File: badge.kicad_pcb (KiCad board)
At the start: 2 copper layers, 65 x 75 mm, 21 parts, among them J1 PMOD_0, J2 PMOD_1, U1 TPS61165

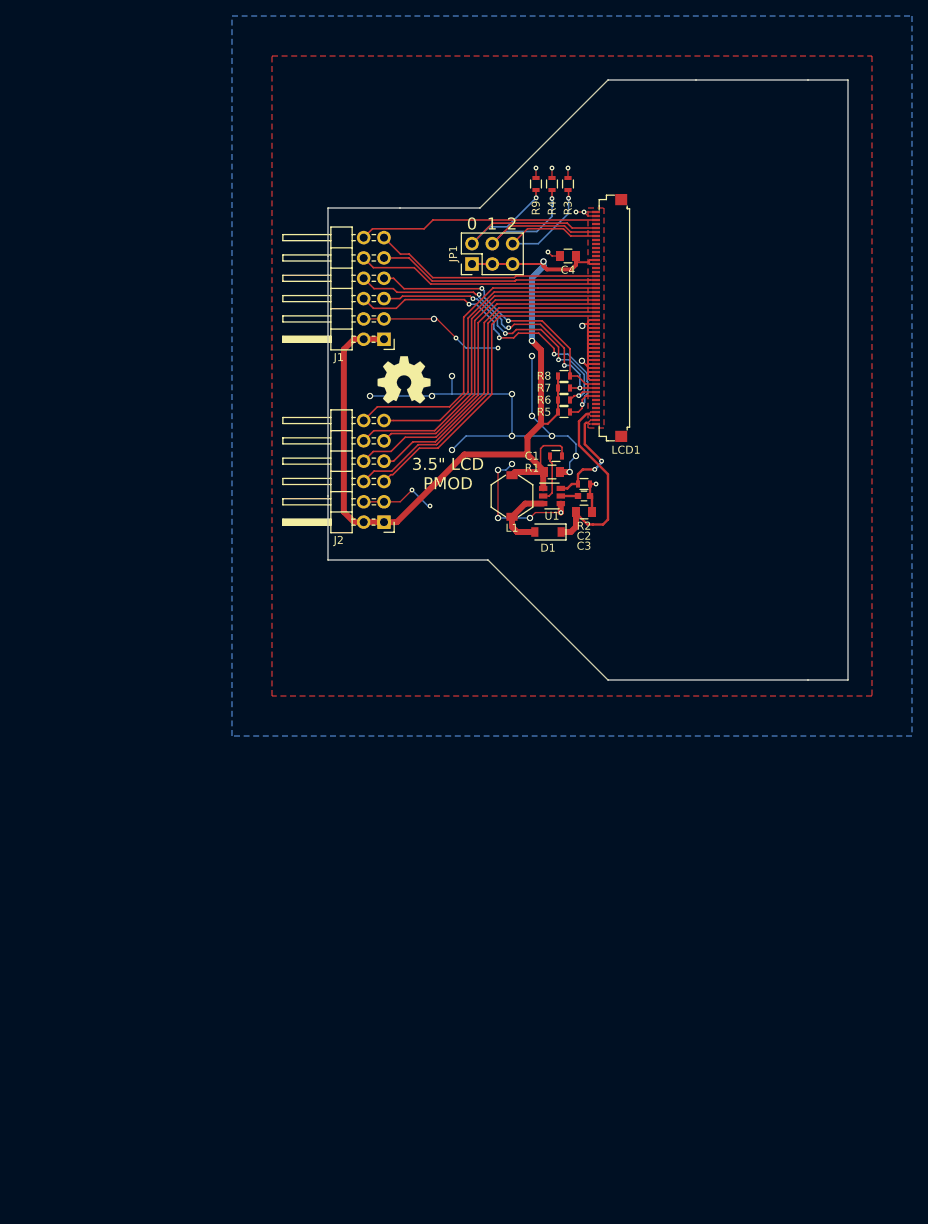
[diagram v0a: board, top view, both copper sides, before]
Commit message: Footprint assignments and initial placement
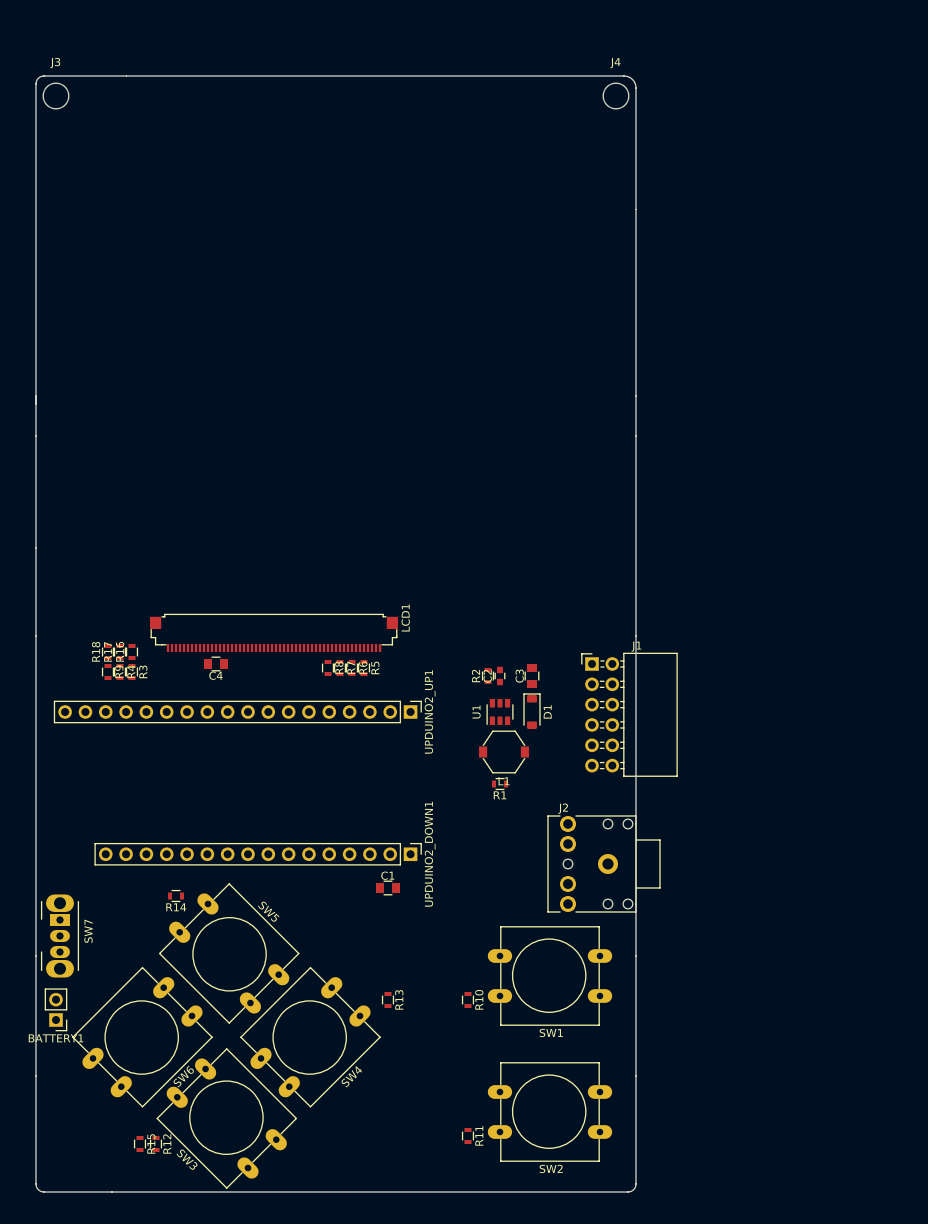
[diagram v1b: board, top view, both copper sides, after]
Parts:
- removed JP1: JMPx3, Pin_Headers:Pin_Header_Straight_2x03_Pitch2.54mm
- removed REF***: OSHW-Symbol_6.7x6mm_SilkScreen, Symbols:OSHW-Symbol_6.7x6mm_SilkScreen
- added BATTERY1: Conn_01x02, Pin_Headers:Pin_Header_Straight_1x02_Pitch2.54mm, F.Cu at (73.0, 150.5)
- added J3: HOLE, Mounting_Holes:MountingHole_3.2mm_M3, F.Cu at (73.0, 35.0)
- added J4: HOLE, Mounting_Holes:MountingHole_3.2mm_M3, F.Cu at (143.0, 35.0)
- added R10: 10K, Resistors_SMD:R_0603, F.Cu at (124.5, 148.0)
- added R11: 10K, Resistors_SMD:R_0603, F.Cu at (124.5, 165.0)
- added R12: 10K, Resistors_SMD:R_0603, F.Cu at (85.5, 166.0)
- added R13: 10K, Resistors_SMD:R_0603, F.Cu at (114.5, 148.0)
- added R14: 10K, Resistors_SMD:R_0603, F.Cu at (88.0, 135.0)
- added R15: 10K, Resistors_SMD:R_0603, F.Cu at (83.5, 166.0)
- added R16: DNP, Resistors_SMD:R_0603, F.Cu at (82.5, 104.5)
- added R17: DNP, Resistors_SMD:R_0603, F.Cu at (81.0, 104.5)
- added R18: 10k, Resistors_SMD:R_0603, F.Cu at (79.5, 104.5)
- added SW1: SW_Push, Buttons_Switches_THT:SW_PUSH-12mm, F.Cu at (141.0, 147.5)
- added SW2: SW_Push, Buttons_Switches_THT:SW_PUSH-12mm, F.Cu at (141.0, 164.5)
- added SW3: SW_Push, Buttons_Switches_THT:SW_PUSH-12mm, F.Cu at (97.0, 169.0)
- added SW4: SW_Push, Buttons_Switches_THT:SW_PUSH-12mm, F.Cu at (111.0, 150.0)
- added SW5: SW_Push, Buttons_Switches_THT:SW_PUSH-12mm, F.Cu at (92.0, 136.0)
- added SW6: SW_Push, Buttons_Switches_THT:SW_PUSH-12mm, F.Cu at (90.0, 150.0)
- added SW7: SW_SPDT, Buttons_Switches_THT:SW_CuK_OS102011MA1QN1_SPDT_Angled, F.Cu at (73.5, 138.0)
- added UPDUINO2_DOWN1: Conn_01x16, Pin_Headers:Pin_Header_Straight_1x16_Pitch2.54mm, F.Cu at (117.3, 129.8)
- added UPDUINO2_UP1: Conn_01x18, Pin_Headers:Pin_Header_Straight_1x18_Pitch2.54mm, F.Cu at (117.3, 112.0)
- J1: value PMOD_0 -> PMOD; footprint Custom Parts:PMOD_2x06_2.54mm -> Custom Parts:Pin_Header_Angled_2x06_Pitch2.54mm_PMOD
- J2: value PMOD_1 -> Audio-Jack-3; footprint Custom Parts:PMOD_2x06_2.54mm -> Custom Parts:AUDIO_JACK_3.5mm
- R9: value 10k -> DNP
- moved R3 81.8 mm to (82.5, 107.0), turned to 270 degrees
- moved R4 81.5 mm to (81.0, 107.0), turned to 270 degrees
- moved R9 81.1 mm to (79.5, 107.0), turned to 270 degrees
- moved C4 67.4 mm to (93.0, 106.0)
- moved LCD1 57.6 mm to (100.2, 103.5), turned to 180 degrees
- moved C1 55.9 mm to (114.5, 134.0)
- moved J2 51.1 mm to (142.0, 131.0)
- moved J1 48.2 mm to (140.0, 106.0), turned to 0 degrees
- moved R8 46.9 mm to (107.0, 106.5), turned to 270 degrees
- moved R7 44.8 mm to (108.5, 106.5), turned to 270 degrees
- moved R6 42.7 mm to (110.0, 106.5), turned to 270 degrees
- moved R1 41.6 mm to (128.5, 121.0), turned to 180 degrees
- moved R5 40.6 mm to (111.5, 106.5), turned to 270 degrees
- moved L1 32.0 mm to (129.0, 117.0), turned to 0 degrees
- moved U1 27.8 mm to (128.5, 112.0), turned to 90 degrees
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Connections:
- net Net-(R1-Pad1) renamed /TPS_CTRL
- J1 pad 1: /DCLK -> /PMOD0
- J1 pad 10: /~RESET -> /PMOD7
- J1 pad 2: /VSYNC -> /PMOD2
- J1 pad 3: /SPDAT -> /PMOD4
- J1 pad 4: /SPENA -> /PMOD6
- J1 pad 7: /DEN -> /PMOD1
- J1 pad 8: /HSYNC -> /PMOD3
- J1 pad 9: /SPCLK -> /PMOD5
- J2 pad 1: /DX6 -> /AUDIO
- J2 pad 2: /DX4 -> /AUDIO
- J2 pad 3: /DX2 -> GND
- LCD1 pad 10: /SPCLK -> Net-(LCD1-Pad10)
- LCD1 pad 11: /SPDAT -> Net-(LCD1-Pad11)
- LCD1 pad 39: Net-(LCD1-Pad39) -> (no net)
- LCD1 pad 40: Net-(LCD1-Pad40) -> (no net)
- LCD1 pad 43: Net-(LCD1-Pad43) -> (no net)
- LCD1 pad 44: Net-(LCD1-Pad44) -> (no net)
- LCD1 pad 45: Net-(LCD1-Pad45) -> (no net)
- LCD1 pad 46: Net-(LCD1-Pad46) -> (no net)
- LCD1 pad 47: Net-(LCD1-Pad47) -> (no net)
- LCD1 pad 5: Net-(LCD1-Pad5) -> (no net)
- LCD1 pad 51: Net-(LCD1-Pad51) -> (no net)
- LCD1 pad 6: Net-(LCD1-Pad6) -> (no net)
- LCD1 pad 7: Net-(LCD1-Pad7) -> (no net)
- LCD1 pad 9: /SPENA -> Net-(LCD1-Pad9)
- R6 pad 1: /SPENA -> Net-(LCD1-Pad9)
- R7 pad 1: /SPCLK -> Net-(LCD1-Pad10)
- R8 pad 1: /SPDAT -> Net-(LCD1-Pad11)
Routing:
- net GND: track 143.0 -> 0.00 mm, vias 30 -> 0
- net +3V3: track 121.3 -> 0.00 mm, vias 2 -> 0
- net /~RESET: track 43.3 -> 0.00 mm, vias 4 -> 0
- net /DX1: track 42.9 -> 0.00 mm
- net /DX3: track 42.5 -> 0.00 mm
- net /DX5: track 42.0 -> 0.00 mm
- net /DX7: track 41.4 -> 0.00 mm
- net /DX0: track 40.2 -> 0.00 mm
- net /DX2: track 39.6 -> 0.00 mm
- net /DX4: track 39.2 -> 0.00 mm
- net /SPCLK: track 39.1 -> 0.00 mm, vias 4 -> 0
- net /DX6: track 38.6 -> 0.00 mm
- net /SPENA: track 37.8 -> 0.00 mm, vias 4 -> 0
- net /SPDAT: track 34.5 -> 0.00 mm, vias 2 -> 0
- net /HSYNC: track 30.4 -> 0.00 mm
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- removed copper zone on B.Cu, net GND
- removed copper zone on F.Cu, net GND
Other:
- board size 65 x 75 mm -> 75 x 139.5 mm
- board text removed: "0"
- board text removed: "1"
- board text removed: "2"
- board text removed: "3.5" LCD PMOD"

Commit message: Routing done and logos added
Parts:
- added J11: ICESTUDIO_LOGO, Custom Parts:ICESTUDIO, B.Cu at (126.8, 82.5)
- added J5: OSHW_LOGO, Symbols:OSHW-Logo2_24.3x20mm_SilkScreen, B.Cu at (126.8, 61.0)
- added J6: ICOTC_LOGO, Custom Parts:ICOTC, B.Cu at (89.2, 79.8)
- added J8: KICAD_LOGO, Symbols:KiCad-Logo_12mm_SilkScreen, B.Cu at (89.2, 61.0)
- moved C1 26.1 mm to (125.4, 110.3), turned to 90 degrees
- moved R1 11.8 mm to (123.7, 110.2), turned to 90 degrees
- moved R16 3.00 mm to (79.5, 104.5)
- moved R18 3.00 mm to (82.5, 104.5)
- moved R3 3.00 mm to (79.5, 107.0)
- moved R9 3.00 mm to (82.5, 107.0)
- moved L1 2.07 mm to (128.4, 115.0)
- moved C2 1.79 mm to (128.5, 105.7)
- moved C3 1.79 mm to (132.5, 105.7)
- moved D1 1.79 mm to (132.5, 110.2)
- moved R2 1.79 mm to (127.0, 105.7)
- moved U1 1.79 mm to (128.5, 110.2)
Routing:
- net GND: track 0.00 -> 423.7 mm, vias 0 -> 57
- net +3V3: track 0.00 -> 401.6 mm, vias 0 -> 10
- net /BUTTON_4: track 0.00 -> 125.3 mm, vias 0 -> 2
- net /BUTTON_5: track 0.00 -> 109.1 mm, vias 0 -> 2
- net /BUTTON_3: track 0.00 -> 86.4 mm
- net /PMOD0: track 0.00 -> 62.1 mm
- net /PMOD1: track 0.00 -> 60.2 mm
- net /BUTTON_2: track 0.00 -> 52.0 mm
- net /PMOD2: track 0.00 -> 51.5 mm
- net /PMOD3: track 0.00 -> 51.2 mm
- net /TPS_CTRL: track 0.00 -> 49.3 mm, vias 0 -> 2
- net /AUDIO: track 0.00 -> 47.2 mm
- net /PMOD5: track 0.00 -> 45.2 mm
- net /PMOD4: track 0.00 -> 44.9 mm
- net /BUTTON_0: track 0.00 -> 42.5 mm
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- added copper zone on B.Cu, net GND
- added copper zone on F.Cu, net GND
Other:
- board size 75 x 139.5 mm -> 75 x 140 mm
- net class Default: clearance 0 -> 0.1524
- rule trace_clearance: 0 -> 0.1524
- board text added: "FPGA 101 Workshop Badge"
- board text added: "POWERED BY"
- board text added: "icoTC"

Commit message: Final tweaks, create gerbers
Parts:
- added J7: OSHPARK_LOGO, Custom Parts:OSHPARK, B.Cu at (126.8, 90.8)
- moved J11 10.0 mm to (126.8, 72.5)
- moved J5 8.50 mm to (126.8, 52.5)
- moved J8 8.50 mm to (89.2, 52.5)
- moved J6 3.50 mm to (89.2, 76.2)
